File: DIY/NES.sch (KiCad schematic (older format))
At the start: 6 parts, among them J1 Conn_01x07, J2 Conn_01x07, J3 DB15_Female, J4 DB25_Male, U1 74AHCT125N, U2 74AHCT125N

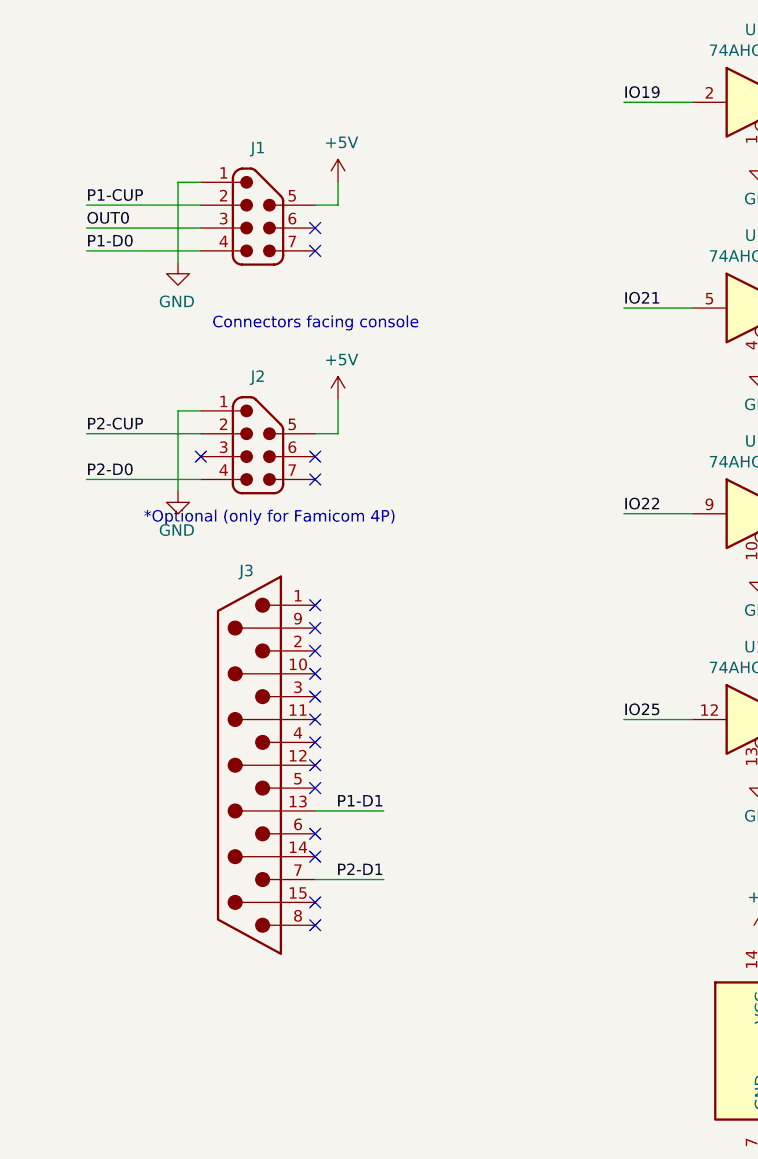
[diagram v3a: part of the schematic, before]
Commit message: Update adapter cable schematics
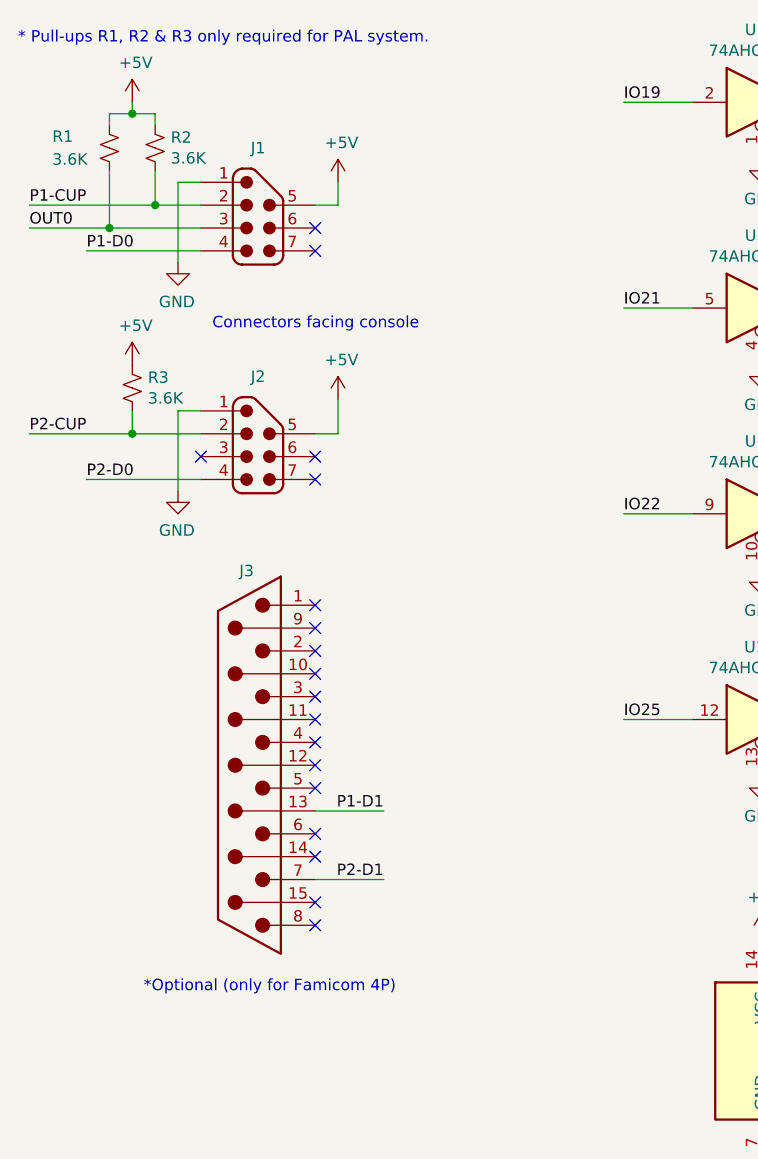
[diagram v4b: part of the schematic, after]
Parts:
- added R1, R2, R3: 3.6K, symbol Device:R_Small_US
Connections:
- net +5V: now also R1.1, R2.1, R3.1
- net OUT0: now also R1.2
- net P1-CUP: now also R2.2
- net P2-CUP: now also R3.2
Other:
- note added: "* Pull-ups R1, R2 & R3 only required for PAL system."
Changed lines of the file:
@@
 $Descr USLetter 11000 8500
 encoding utf-8
-Sheet 3 7
+Sheet 3 10
 Title "BlueRetro - Famicom/NES adapter cable"
-Date "2020-10-02"
-Rev "v1.2"
+Date "2020-11-03"
+Rev "v1.2.1"
 Comp "©2020 Jacques Gagnon, licensed under CC-BY-4.0"
 Comment1 ""
@@
 P 6900 4350
 AR Path="/5F127084/5F23BD1E" Ref="#PWR?"  Part="1"
-AR Path="/5F1E85DD/5F23BD1E" Ref="#PWR?"  Part="1"
-F 0 "#PWR?" H 6900 4100 50  0001 C CNN
+AR Path="/5F1E85DD/5F23BD1E" Ref="#PWR060"  Part="1"
+F 0 "#PWR060" H 6900 4100 50  0001 C CNN
 F 1 "GND" H 6905 4177 50  0000 C CNN
 F 2 "" H 6900 4350 50  0001 C CNN
@@
 P 6900 3450
 AR Path="/5F127084/5F23BD24" Ref="#PWR?"  Part="1"
-AR Path="/5F1E85DD/5F23BD24" Ref="#PWR?"  Part="1"
-F 0 "#PWR?" H 6900 3200 50  0001 C CNN
+AR Path="/5F1E85DD/5F23BD24" Ref="#PWR059"  Part="1"
+F 0 "#PWR059" H 6900 3200 50  0001 C CNN
 F 1 "GND" H 6905 3277 50  0000 C CNN
 F 2 "" H 6900 3450 50  0001 C CNN
@@
 P 6900 1650
 AR Path="/5F127084/5F23BD2A" Ref="#PWR?"  Part="1"
-AR Path="/5F1E85DD/5F23BD2A" Ref="#PWR?"  Part="1"
-F 0 "#PWR?" H 6900 1400 50  0001 C CNN
+AR Path="/5F1E85DD/5F23BD2A" Ref="#PWR057"  Part="1"
+F 0 "#PWR057" H 6900 1400 50  0001 C CNN
 F 1 "GND" H 6905 1477 50  0000 C CNN
 F 2 "" H 6900 1650 50  0001 C CNN
@@
 P 6900 2550
 AR Path="/5F127084/5F23BD30" Ref="#PWR?"  Part="1"
-AR Path="/5F1E85DD/5F23BD30" Ref="#PWR?"  Part="1"
-F 0 "#PWR?" H 6900 2300 50  0001 C CNN
+AR Path="/5F1E85DD/5F23BD30" Ref="#PWR058"  Part="1"
+F 0 "#PWR058" H 6900 2300 50  0001 C CNN
 F 1 "GND" H 6905 2377 50  0000 C CNN
 F 2 "" H 6900 2550 50  0001 C CNN
@@
 P 4150 2500
 AR Path="/5F127084/5F23BD36" Ref="#PWR?"  Part="1"
-AR Path="/5F1E85DD/5F23BD36" Ref="#PWR?"  Part="1"
-F 0 "#PWR?" H 4150 2250 50  0001 C CNN
+AR Path="/5F1E85DD/5F23BD36" Ref="#PWR049"  Part="1"
+F 0 "#PWR049" H 4150 2250 50  0001 C CNN
 F 1 "GND" H 4155 2327 50  0000 C CNN
 F 2 "" H 4150 2500 50  0001 C CNN
@@
 P 4150 4300
 AR Path="/5F127084/5F23BD3C" Ref="#PWR?"  Part="1"
-AR Path="/5F1E85DD/5F23BD3C" Ref="#PWR?"  Part="1"
-F 0 "#PWR?" H 4150 4050 50  0001 C CNN
+AR Path="/5F1E85DD/5F23BD3C" Ref="#PWR051"  Part="1"
+F 0 "#PWR051" H 4150 4050 50  0001 C CNN
 F 1 "GND" H 4155 4127 50  0000 C CNN
 F 2 "" H 4150 4300 50  0001 C CNN
@@
 P 4150 1600
 AR Path="/5F127084/5F23BD42" Ref="#PWR?"  Part="1"
-AR Path="/5F1E85DD/5F23BD42" Ref="#PWR?"  Part="1"
-F 0 "#PWR?" H 4150 1350 50  0001 C CNN
+AR Path="/5F1E85DD/5F23BD42" Ref="#PWR048"  Part="1"
+F 0 "#PWR048" H 4150 1350 50  0001 C CNN
 F 1 "GND" H 4155 1427 50  0000 C CNN
 F 2 "" H 4150 1600 50  0001 C CNN
@@
 P 4150 3400
 AR Path="/5F127084/5F23BD48" Ref="#PWR?"  Part="1"
-AR Path="/5F1E85DD/5F23BD48" Ref="#PWR?"  Part="1"
-F 0 "#PWR?" H 4150 3150 50  0001 C CNN
+AR Path="/5F1E85DD/5F23BD48" Ref="#PWR050"  Part="1"
+F 0 "#PWR050" H 4150 3150 50  0001 C CNN
 F 1 "GND" H 4155 3227 50  0000 C CNN
 F 2 "" H 4150 3400 50  0001 C CNN
@@
 P 6550 6050
 AR Path="/5F127084/5F23BD7E" Ref="#PWR?"  Part="1"
-AR Path="/5F1E85DD/5F23BD7E" Ref="#PWR?"  Part="1"
-F 0 "#PWR?" H 6550 5800 50  0001 C CNN
+AR Path="/5F1E85DD/5F23BD7E" Ref="#PWR056"  Part="1"
+F 0 "#PWR056" H 6550 5800 50  0001 C CNN
 F 1 "GND" H 6555 5877 50  0000 C CNN
 F 2 "" H 6550 6050 50  0001 C CNN
@@
 P 4150 6000
 AR Path="/5F127084/5F23BD90" Ref="#PWR?"  Part="1"
-AR Path="/5F1E85DD/5F23BD90" Ref="#PWR?"  Part="1"
-F 0 "#PWR?" H 4150 5750 50  0001 C CNN
+AR Path="/5F1E85DD/5F23BD90" Ref="#PWR053"  Part="1"
+F 0 "#PWR053" H 4150 5750 50  0001 C CNN
 F 1 "GND" H 4155 5827 50  0000 C CNN
 F 2 "" H 4150 6000 50  0001 C CNN
@@
 P 6550 5050
 AR Path="/5F127084/5F23BD96" Ref="#PWR?"  Part="1"
-AR Path="/5F1E85DD/5F23BD96" Ref="#PWR?"  Part="1"
-F 0 "#PWR?" H 6550 4900 50  0001 C CNN
+AR Path="/5F1E85DD/5F23BD96" Ref="#PWR055"  Part="1"
+F 0 "#PWR055" H 6550 4900 50  0001 C CNN
 F 1 "+3.3V" H 6565 5223 50  0000 C CNN
 F 2 "" H 6550 5050 50  0001 C CNN
@@
 P 4150 5000
 AR Path="/5F127084/5F23BDA2" Ref="#PWR?"  Part="1"
-AR Path="/5F1E85DD/5F23BDA2" Ref="#PWR?"  Part="1"
-F 0 "#PWR?" H 4150 4850 50  0001 C CNN
+AR Path="/5F1E85DD/5F23BDA2" Ref="#PWR052"  Part="1"
+F 0 "#PWR052" H 4150 4850 50  0001 C CNN
 F 1 "+5V" H 4165 5173 50  0000 C CNN
 F 2 "" H 4150 5000 50  0001 C CNN
@@
 P 1600 2050
 AR Path="/5F127084/5F23BE05" Ref="#PWR?"  Part="1"
-AR Path="/5F1E85DD/5F23BE05" Ref="#PWR?"  Part="1"
-F 0 "#PWR?" H 1600 1800 50  0001 C CNN
+AR Path="/5F1E85DD/5F23BE05" Ref="#PWR044"  Part="1"
+F 0 "#PWR044" H 1600 1800 50  0001 C CNN
 F 1 "GND" H 1605 1877 50  0000 C CNN
 F 2 "" H 1600 2050 50  0001 C CNN
@@
 P 1600 3050
 AR Path="/5F127084/5F23BE0B" Ref="#PWR?"  Part="1"
-AR Path="/5F1E85DD/5F23BE0B" Ref="#PWR?"  Part="1"
-F 0 "#PWR?" H 1600 2800 50  0001 C CNN
+AR Path="/5F1E85DD/5F23BE0B" Ref="#PWR045"  Part="1"
+F 0 "#PWR045" H 1600 2800 50  0001 C CNN
 F 1 "GND" H 1605 2877 50  0000 C CNN
 F 2 "" H 1600 3050 50  0001 C CNN
@@
 P 2300 2650
 AR Path="/5F127084/5F23BE11" Ref="#PWR?"  Part="1"
-AR Path="/5F1E85DD/5F23BE11" Ref="#PWR?"  Part="1"
-F 0 "#PWR?" H 2300 2500 50  0001 C CNN
+AR Path="/5F1E85DD/5F23BE11" Ref="#PWR047"  Part="1"
+F 0 "#PWR047" H 2300 2500 50  0001 C CNN
 F 1 "+5V" H 2315 2823 50  0000 C CNN
 F 2 "" H 2300 2650 50  0001 C CNN
@@
 P 2300 1700
 AR Path="/5F127084/5F23BE17" Ref="#PWR?"  Part="1"
-AR Path="/5F1E85DD/5F23BE17" Ref="#PWR?"  Part="1"
-F 0 "#PWR?" H 2300 1550 50  0001 C CNN
+AR Path="/5F1E85DD/5F23BE17" Ref="#PWR046"  Part="1"
+F 0 "#PWR046" H 2300 1550 50  0001 C CNN
 F 1 "+5V" H 2315 1873 50  0000 C CNN
 F 2 "" H 2300 1700 50  0001 C CNN
@@
 Wire Wire Line
 	2200 4750 2500 4750
-Text Notes 1450 3200 0    50   ~ 0
+Text Notes 1450 5250 0    50   ~ 0
 *Optional (only for Famicom 4P)
 NoConn ~ 2200 3550
@@
 Wire Wire Line
 	1700 2700 1600 2700
-Text Label 1200 2800 0    50   ~ 0
+Text Label 950  2800 0    50   ~ 0
 P2-CUP
-Wire Wire Line
-	1700 2800 1200 2800
 Wire Wire Line
 	1700 3000 1200 3000
@@
 Wire Wire Line
 	1700 1700 1600 1700
-Wire Wire Line
-	1700 1800 1200 1800
-Text Label 1200 1800 0    50   ~ 0
+Text Label 950  1800 0    50   ~ 0
 P1-CUP
-Text Label 1200 1900 0    50   ~ 0
+Text Label 950  1900 0    50   ~ 0
 OUT0
 Text Label 1200 2000 0    50   ~ 0
@@
 P 6250 4100
 AR Path="/5F127084/5F260E90" Ref="#PWR?"  Part="1"
-AR Path="/5F1E85DD/5F260E90" Ref="#PWR?"  Part="1"
-F 0 "#PWR?" H 6250 3850 50  0001 C CNN
+AR Path="/5F1E85DD/5F260E90" Ref="#PWR054"  Part="1"
+F 0 "#PWR054" H 6250 3850 50  0001 C CNN
 F 1 "GND" H 6255 3927 50  0000 C CNN
 F 2 "" H 6250 4100 50  0001 C CNN
@@
 P 9350 1300
 AR Path="/5F127084/5F70CF77" Ref="#PWR?"  Part="1"
-AR Path="/5F1E85DD/5F70CF77" Ref="#PWR?"  Part="1"
+AR Path="/5F1E85DD/5F70CF77" Ref="#PWR063"  Part="1"
 AR Path="/5F2C5C0D/5F70CF77" Ref="#PWR?"  Part="1"
-F 0 "#PWR?" H 9350 1150 50  0001 C CNN
+F 0 "#PWR063" H 9350 1150 50  0001 C CNN
 F 1 "+5V" H 9365 1473 50  0000 C CNN
 F 2 "" H 9350 1300 50  0001 C CNN
@@
 P 9250 3900
 AR Path="/5F127084/5F70CF7D" Ref="#PWR?"  Part="1"
-AR Path="/5F1E85DD/5F70CF7D" Ref="#PWR?"  Part="1"
+AR Path="/5F1E85DD/5F70CF7D" Ref="#PWR062"  Part="1"
 AR Path="/5F2C5C0D/5F70CF7D" Ref="#PWR?"  Part="1"
-F 0 "#PWR?" H 9250 3650 50  0001 C CNN
+F 0 "#PWR062" H 9250 3650 50  0001 C CNN
 F 1 "GND" H 9255 3727 50  0000 C CNN
 F 2 "" H 9250 3900 50  0001 C CNN
@@
 P 9050 2350
 AR Path="/5F127084/5F70CF87" Ref="#PWR?"  Part="1"
-AR Path="/5F1E85DD/5F70CF87" Ref="#PWR?"  Part="1"
+AR Path="/5F1E85DD/5F70CF87" Ref="#PWR061"  Part="1"
 AR Path="/5F2C5C0D/5F70CF87" Ref="#PWR?"  Part="1"
-F 0 "#PWR?" H 9050 2200 50  0001 C CNN
+F 0 "#PWR061" H 9050 2200 50  0001 C CNN
 F 1 "+3.3V" H 9065 2523 50  0000 C CNN
 F 2 "" H 9050 2350 50  0001 C CNN
@@
 Wire Wire Line
 	1700 2000 1200 2000
-Wire Wire Line
-	1700 1900 1200 1900
 Wire Wire Line
 	1600 1700 1600 2050
@@
 Wire Wire Line
 	2300 2800 2300 2650
+$Comp
+L Device:R_Small_US R2
+U 1 1 5FC2552B
+P 1500 1550
+F 0 "R2" H 1568 1596 50  0000 L CNN
+F 1 "3.6K" H 1568 1505 50  0000 L CNN
+F 2 "" H 1500 1550 50  0001 C CNN
+F 3 "~" H 1500 1550 50  0001 C CNN
+	1    1500 1550
+	1    0    0    -1
+$EndComp
+Wire Wire Line
+	950  1900 1300 1900
+Wire Wire Line
+	950  2800 1400 2800
+$Comp
+L Device:R_Small_US R1
+U 1 1 5FC33CA0
+P 1300 1550
+F 0 "R1" H 1050 1600 50  0000 L CNN
+F 1 "3.6K" H 1050 1500 50  0000 L CNN
+F 2 "" H 1300 1550 50  0001 C CNN
+F 3 "~" H 1300 1550 50  0001 C CNN
+	1    1300 1550
+	1    0    0    -1
+$EndComp
+$Comp
+L Device:R_Small_US R3
+U 1 1 5FC3415F
+P 1400 2600
+F 0 "R3" H 1468 2646 50  0000 L CNN
+F 1 "3.6K" H 1468 2555 50  0000 L CNN
+F 2 "" H 1400 2600 50  0001 C CNN
+F 3 "~" H 1400 2600 50  0001 C CNN
+	1    1400 2600
+	1    0    0    -1
+$EndComp
+$Comp
+L power:+5V #PWR?
+U 1 1 5FC3494B
+P 1400 2500
+AR Path="/5F127084/5FC3494B" Ref="#PWR?"  Part="1"
+AR Path="/5F1E85DD/5FC3494B" Ref="#PWR?"  Part="1"
+F 0 "#PWR?" H 1400 2350 50  0001 C CNN
+F 1 "+5V" H 1415 2673 50  0000 C CNN
+F 2 "" H 1400 2500 50  0001 C CNN
+F 3 "" H 1400 2500 50  0001 C CNN
+	1    1400 2500
+	1    0    0    -1
+$EndComp
+$Comp
+L power:+5V #PWR?
+U 1 1 5FC34F45
+P 1400 1350
+AR Path="/5F127084/5FC34F45" Ref="#PWR?"  Part="1"
+AR Path="/5F1E85DD/5FC34F45" Ref="#PWR?"  Part="1"
+F 0 "#PWR?" H 1400 1200 50  0001 C CNN
+F 1 "+5V" H 1415 1523 50  0000 C CNN
+F 2 "" H 1400 1350 50  0001 C CNN
+F 3 "" H 1400 1350 50  0001 C CNN
+	1    1400 1350
+	1    0    0    -1
+$EndComp
+Wire Wire Line
+	1400 2700 1400 2800
+Connection ~ 1400 2800
+Wire Wire Line
+	1400 2800 1700 2800
+Wire Wire Line
+	1300 1450 1300 1400
+Wire Wire Line
+	1300 1400 1400 1400
+Wire Wire Line
+	1400 1400 1400 1350
+Wire Wire Line
+	1400 1400 1500 1400
+Wire Wire Line
+	1500 1400 1500 1450
+Connection ~ 1400 1400
+Wire Wire Line
+	950  1800 1500 1800
+Wire Wire Line
+	1500 1650 1500 1800
+Connection ~ 1500 1800
+Wire Wire Line
+	1500 1800 1700 1800
+Wire Wire Line
+	1300 1650 1300 1900
+Connection ~ 1300 1900
+Wire Wire Line
+	1300 1900 1700 1900
+Text Notes 900  1100 0    50   ~ 0
+* Pull-ups R1, R2 & R3 only required for PAL system.
 $EndSCHEMATC
